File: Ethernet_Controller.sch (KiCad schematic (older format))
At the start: 33 parts, among them J1 5-2337992-8, U1 RTL8111H, Y1 ABM8G-25.000MHZ-18-D2Y-T

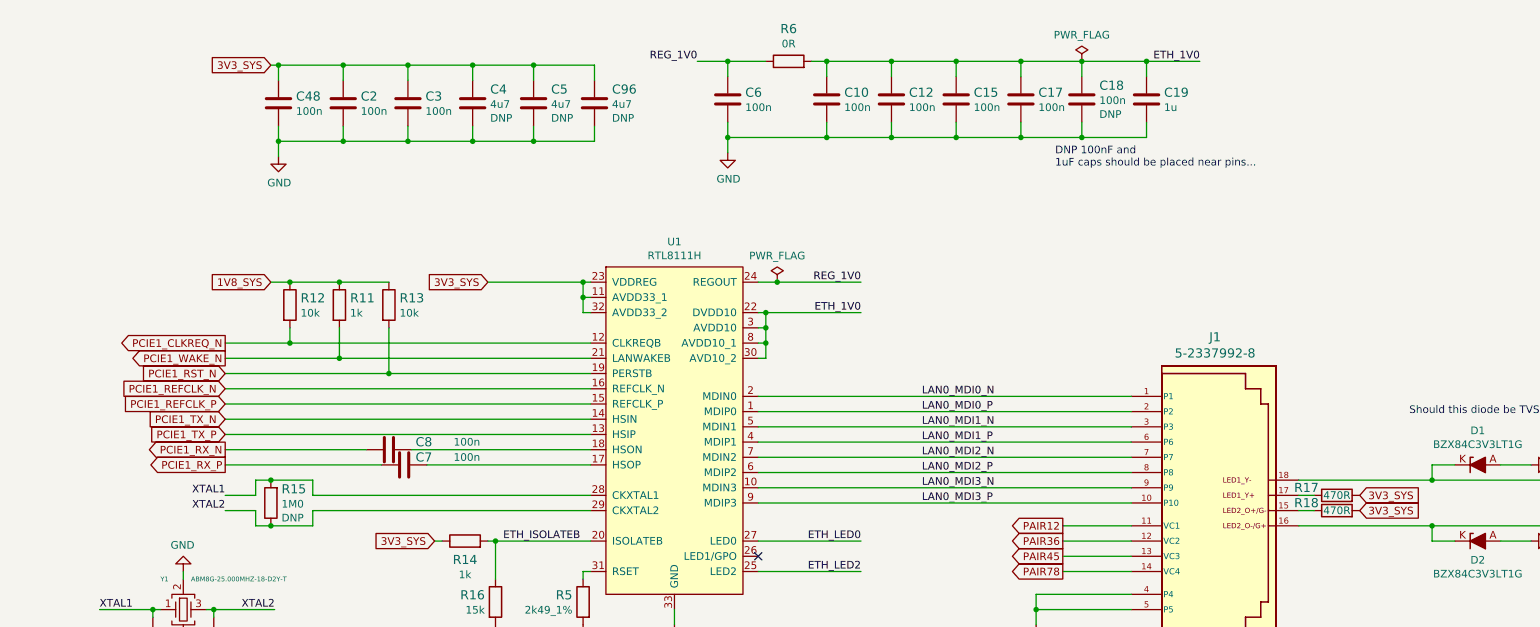
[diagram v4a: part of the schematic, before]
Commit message: Add ferrite bead to 3V3 path to ethernet, update power labels
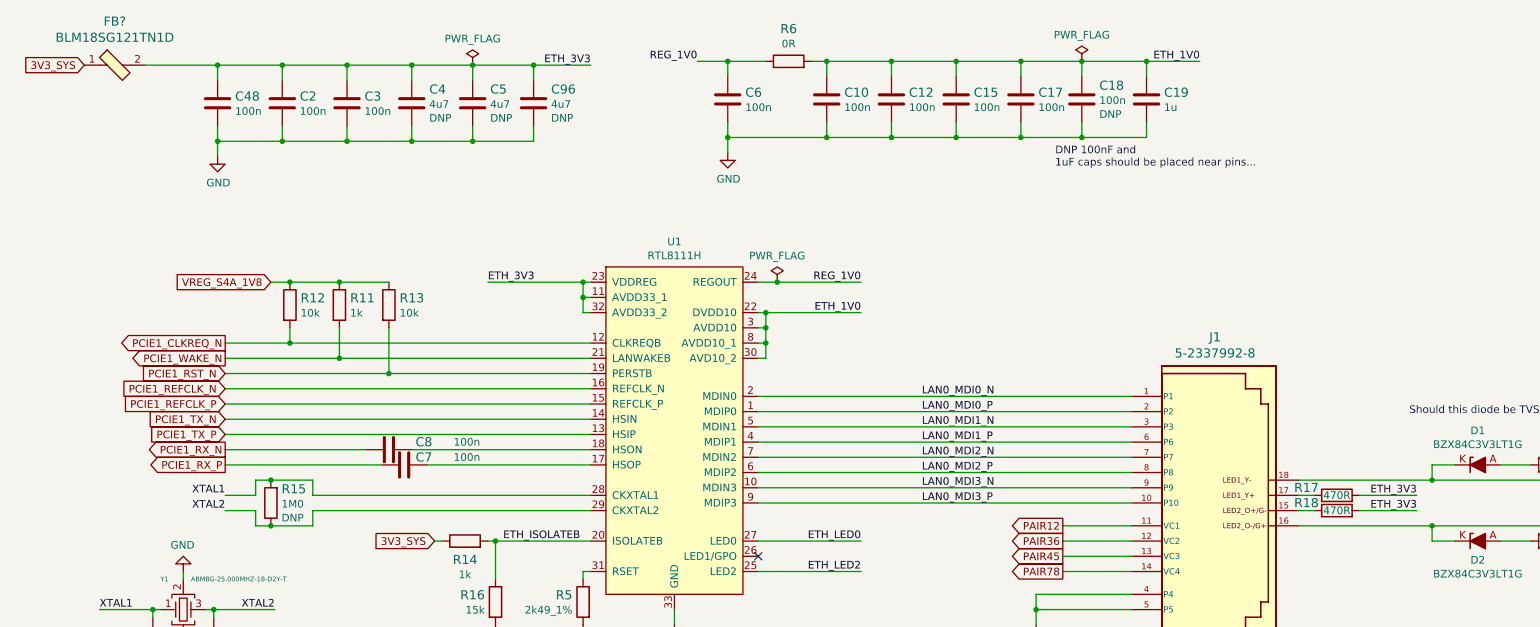
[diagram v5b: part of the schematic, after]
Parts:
- added FB?: BLM18SG121TN1D, sa800u-baseboard-hw-footprints:0603-res, symbol sa800u-baseboard-hw:BLM18SG121TN1D
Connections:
- net 3V3_SYS: now also FB?.1; no longer C2.1, C3.1, C4.1, C48.1, C5.1, C96.1, R17.2, R18.2, U1.11 (AVDD33_1), U1.23 (VDDREG), U1.32 (AVDD33_2)
- net 1V8_SYS renamed VREG_S4A_1V8
- new net ETH_3V3: C2.1, C3.1, C4.1, C48.1, C5.1, C96.1, FB?.2, R17.2, R18.2, U1.11 (AVDD33_1), U1.23 (VDDREG), U1.32 (AVDD33_2)
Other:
- moved on the sheet: C2, C3, C4, C48, C5, C96
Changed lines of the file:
@@
 Wire Wire Line
 	11700 6025 11600 6025
-Text GLabel 12000 5925 2    50   Input ~ 0
-3V3_SYS
-Text GLabel 12000 6025 2    50   Input ~ 0
-3V3_SYS
 Wire Wire Line
 	12475 6225 12475 6125
@@
 Text Notes 10675 7300 0    50   ~ 10
 Possible replacement:\nhttps://www.l-p.com/products/457392.htm
-Text GLabel 4850 3100 0    50   Input ~ 0
+Text GLabel 3625 3100 0    50   Input ~ 0
 3V3_SYS
 $Comp
 L sa800u-baseboard-hw:C_100n_0402 C2
 U 1 1 62C66184
-P 5325 3350
-F 0 "C2" H 5440 3395 60  0000 L CNN
-F 1 "C_100n_0402" H 5325 3200 60  0001 C CNN
-F 2 "sa800u-baseboard-hw-footprints:0402-cap" H 5525 3550 60  0001 L CNN
-F 3 "" H 5325 3350 50  0001 C CNN
-F 4 "Walsin" H 5525 3750 60  0001 L CNN "Manufacturer"
-F 5 "0402X104K6R3CT" H 5525 3650 60  0001 L CNN "MPN"
-F 6 "100n" H 5440 3297 50  0000 L CNN "Val"
-	1    5325 3350
+P 4925 3350
+F 0 "C2" H 5040 3395 60  0000 L CNN
+F 1 "C_100n_0402" H 4925 3200 60  0001 C CNN
+F 2 "sa800u-baseboard-hw-footprints:0402-cap" H 5125 3550 60  0001 L CNN
+F 3 "" H 4925 3350 50  0001 C CNN
+F 4 "Walsin" H 5125 3750 60  0001 L CNN "Manufacturer"
+F 5 "0402X104K6R3CT" H 5125 3650 60  0001 L CNN "MPN"
+F 6 "100n" H 5040 3297 50  0000 L CNN "Val"
+	1    4925 3350
 	1    0    0    -1
 $EndComp
@@
 L sa800u-baseboard-hw:C_100n_0402 C3
 U 1 1 62C66AB1
-P 5750 3350
-F 0 "C3" H 5865 3395 60  0000 L CNN
-F 1 "C_100n_0402" H 5750 3200 60  0001 C CNN
-F 2 "sa800u-baseboard-hw-footprints:0402-cap" H 5950 3550 60  0001 L CNN
-F 3 "" H 5750 3350 50  0001 C CNN
-F 4 "Walsin" H 5950 3750 60  0001 L CNN "Manufacturer"
-F 5 "0402X104K6R3CT" H 5950 3650 60  0001 L CNN "MPN"
-F 6 "100n" H 5865 3297 50  0000 L CNN "Val"
-	1    5750 3350
+P 5350 3350
+F 0 "C3" H 5465 3395 60  0000 L CNN
+F 1 "C_100n_0402" H 5350 3200 60  0001 C CNN
+F 2 "sa800u-baseboard-hw-footprints:0402-cap" H 5550 3550 60  0001 L CNN
+F 3 "" H 5350 3350 50  0001 C CNN
+F 4 "Walsin" H 5550 3750 60  0001 L CNN "Manufacturer"
+F 5 "0402X104K6R3CT" H 5550 3650 60  0001 L CNN "MPN"
+F 6 "100n" H 5465 3297 50  0000 L CNN "Val"
+	1    5350 3350
 	1    0    0    -1
 $EndComp
@@
 L sa800u-baseboard-hw:C_4u7_0402 C4
 U 1 1 62C67F6F
+P 5775 3350
+F 0 "C4" H 5890 3441 60  0000 L CNN
+F 1 "C_4u7_0402" H 5775 3200 60  0001 C CNN
+F 2 "sa800u-baseboard-hw-footprints:0402-cap" H 5975 3550 60  0001 L CNN
+F 3 "" H 5775 3350 50  0001 C CNN
+F 4 "MURATA" H 5975 3750 60  0001 L CNN "Manufacturer"
+F 5 "GRM155R61A475MEAAD" H 5975 3650 60  0001 L CNN "MPN"
+F 6 "4u7" H 5890 3343 50  0000 L CNN "Val"
+F 7 "DNP" H 5890 3252 50  0000 L CNN "DNP"
+	1    5775 3350
+	1    0    0    -1
+$EndComp
+$Comp
+L sa800u-baseboard-hw:C_4u7_0402 C5
+U 1 1 62C68893
 P 6175 3350
-F 0 "C4" H 6290 3441 60  0000 L CNN
+F 0 "C5" H 6290 3441 60  0000 L CNN
 F 1 "C_4u7_0402" H 6175 3200 60  0001 C CNN
 F 2 "sa800u-baseboard-hw-footprints:0402-cap" H 6375 3550 60  0001 L CNN
@@
 	1    0    0    -1
 $EndComp
-$Comp
-L sa800u-baseboard-hw:C_4u7_0402 C5
-U 1 1 62C68893
-P 6575 3350
-F 0 "C5" H 6690 3441 60  0000 L CNN
-F 1 "C_4u7_0402" H 6575 3200 60  0001 C CNN
-F 2 "sa800u-baseboard-hw-footprints:0402-cap" H 6775 3550 60  0001 L CNN
-F 3 "" H 6575 3350 50  0001 C CNN
-F 4 "MURATA" H 6775 3750 60  0001 L CNN "Manufacturer"
-F 5 "GRM155R61A475MEAAD" H 6775 3650 60  0001 L CNN "MPN"
-F 6 "4u7" H 6690 3343 50  0000 L CNN "Val"
-F 7 "DNP" H 6690 3252 50  0000 L CNN "DNP"
-	1    6575 3350
-	1    0    0    -1
-$EndComp
-Wire Wire Line
-	5750 3100 5750 3200
-Wire Wire Line
-	5325 3100 5325 3200
+Wire Wire Line
+	5350 3100 5350 3200
+Wire Wire Line
+	4925 3100 4925 3200
+Wire Wire Line
+	5775 3100 5775 3200
 Wire Wire Line
 	6175 3100 6175 3200
 Wire Wire Line
-	6575 3100 6575 3200
-Wire Wire Line
-	5325 3500 5325 3600
-Wire Wire Line
-	5750 3600 5750 3500
+	4925 3500 4925 3600
+Wire Wire Line
+	5350 3600 5350 3500
+Wire Wire Line
+	5775 3500 5775 3600
 Wire Wire Line
 	6175 3500 6175 3600
 Wire Wire Line
-	6575 3500 6575 3600
-Wire Wire Line
-	4900 3600 4900 3700
+	4500 3600 4500 3700
 $Comp
 L sa800u-baseboard-hw:GND #PWR02
 U 1 1 62C92996
-P 4900 3700
-F 0 "#PWR02" H 4900 3450 50  0001 C CNN
-F 1 "GND" H 4905 3527 50  0000 C CNN
-F 2 "" H 4900 3700 50  0001 C CNN
-F 3 "" H 4900 3700 50  0001 C CNN
-	1    4900 3700
+P 4500 3700
+F 0 "#PWR02" H 4500 3450 50  0001 C CNN
+F 1 "GND" H 4505 3527 50  0000 C CNN
+F 2 "" H 4500 3700 50  0001 C CNN
+F 3 "" H 4500 3700 50  0001 C CNN
+	1    4500 3700
 	1    0    0    -1
 $EndComp
@@
 L sa800u-baseboard-hw:C_100n_0402 C48
 U 1 1 61E50090
-P 4900 3350
-F 0 "C48" H 5015 3395 60  0000 L CNN
-F 1 "C_100n_0402" H 4900 3200 60  0001 C CNN
-F 2 "sa800u-baseboard-hw-footprints:0402-cap" H 5100 3550 60  0001 L CNN
-F 3 "" H 4900 3350 50  0001 C CNN
-F 4 "Walsin" H 5100 3750 60  0001 L CNN "Manufacturer"
-F 5 "0402X104K6R3CT" H 5100 3650 60  0001 L CNN "MPN"
-F 6 "100n" H 5015 3297 50  0000 L CNN "Val"
-	1    4900 3350
-	1    0    0    -1
-$EndComp
-Wire Wire Line
-	4900 3100 4900 3200
-Wire Wire Line
-	4900 3500 4900 3600
-Connection ~ 4900 3600
-Wire Wire Line
-	4850 3100 4900 3100
-Connection ~ 4900 3100
-Connection ~ 5325 3100
-Connection ~ 6175 3600
-Wire Wire Line
-	4900 3100 5325 3100
-Wire Wire Line
-	4900 3600 5325 3600
-Connection ~ 5750 3100
-Wire Wire Line
-	5325 3100 5750 3100
-Wire Wire Line
-	5325 3600 5750 3600
-Connection ~ 5325 3600
-Connection ~ 6175 3100
-Wire Wire Line
-	5750 3100 6175 3100
-Wire Wire Line
-	5750 3600 6175 3600
-Connection ~ 5750 3600
-Wire Wire Line
-	6175 3600 6575 3600
-Wire Wire Line
-	6175 3100 6575 3100
+P 4500 3350
+F 0 "C48" H 4615 3395 60  0000 L CNN
+F 1 "C_100n_0402" H 4500 3200 60  0001 C CNN
+F 2 "sa800u-baseboard-hw-footprints:0402-cap" H 4700 3550 60  0001 L CNN
+F 3 "" H 4500 3350 50  0001 C CNN
+F 4 "Walsin" H 4700 3750 60  0001 L CNN "Manufacturer"
+F 5 "0402X104K6R3CT" H 4700 3650 60  0001 L CNN "MPN"
+F 6 "100n" H 4615 3297 50  0000 L CNN "Val"
+	1    4500 3350
+	1    0    0    -1
+$EndComp
+Wire Wire Line
+	4500 3100 4500 3200
+Wire Wire Line
+	4500 3500 4500 3600
+Connection ~ 4500 3600
+Connection ~ 4500 3100
+Connection ~ 4925 3100
+Connection ~ 5775 3600
+Wire Wire Line
+	4500 3100 4925 3100
+Wire Wire Line
+	4500 3600 4925 3600
+Connection ~ 5350 3100
+Wire Wire Line
+	4925 3100 5350 3100
+Wire Wire Line
+	4925 3600 5350 3600
+Connection ~ 4925 3600
+Connection ~ 5775 3100
+Wire Wire Line
+	5350 3100 5775 3100
+Wire Wire Line
+	5350 3600 5775 3600
+Connection ~ 5350 3600
+Wire Wire Line
+	5775 3600 6175 3600
+Wire Wire Line
+	5775 3100 6175 3100
 $Comp
 L sa800u-baseboard-hw:C_4u7_0402 C96
 U 1 1 61EB43EC
-P 6975 3350
-F 0 "C96" H 7090 3441 60  0000 L CNN
-F 1 "C_4u7_0402" H 6975 3200 60  0001 C CNN
-F 2 "sa800u-baseboard-hw-footprints:0402-cap" H 7175 3550 60  0001 L CNN
-F 3 "" H 6975 3350 50  0001 C CNN
-F 4 "MURATA" H 7175 3750 60  0001 L CNN "Manufacturer"
-F 5 "GRM155R61A475MEAAD" H 7175 3650 60  0001 L CNN "MPN"
-F 6 "4u7" H 7090 3343 50  0000 L CNN "Val"
-F 7 "DNP" H 7090 3252 50  0000 L CNN "DNP"
-	1    6975 3350
-	1    0    0    -1
-$EndComp
-Wire Wire Line
-	6975 3100 6975 3200
-Wire Wire Line
-	6975 3500 6975 3600
-Wire Wire Line
-	6575 3600 6975 3600
-Wire Wire Line
-	6575 3100 6975 3100
-Connection ~ 6575 3100
-Connection ~ 6575 3600
+P 6575 3350
+F 0 "C96" H 6690 3441 60  0000 L CNN
+F 1 "C_4u7_0402" H 6575 3200 60  0001 C CNN
+F 2 "sa800u-baseboard-hw-footprints:0402-cap" H 6775 3550 60  0001 L CNN
+F 3 "" H 6575 3350 50  0001 C CNN
+F 4 "MURATA" H 6775 3750 60  0001 L CNN "Manufacturer"
+F 5 "GRM155R61A475MEAAD" H 6775 3650 60  0001 L CNN "MPN"
+F 6 "4u7" H 6690 3343 50  0000 L CNN "Val"
+F 7 "DNP" H 6690 3252 50  0000 L CNN "DNP"
+	1    6575 3350
+	1    0    0    -1
+$EndComp
+Wire Wire Line
+	6575 3100 6575 3200
+Wire Wire Line
+	6575 3500 6575 3600
+Wire Wire Line
+	6175 3600 6575 3600
+Wire Wire Line
+	6175 3100 6575 3100
+Connection ~ 6175 3100
+Connection ~ 6175 3600
 $Comp
 L sa800u-baseboard-hw:C_100n_0402 C10
@@
 	0    -1   1    0
 $EndComp
-Text GLabel 6275 4525 0    50   Input ~ 0
-3V3_SYS
 $Comp
 L sa800u-baseboard-hw:RTL8111H U1
@@
 	0    1    1    0
 $EndComp
-Text GLabel 4850 4525 0    50   Input ~ 0
-1V8_SYS
 $Comp
 L sa800u-baseboard-hw:R_10k_0402 R13
@@
 Wire Wire Line
 	8050 5875 10500 5875
+Text GLabel 4850 4525 0    50   Input ~ 0
+VREG_S4A_1V8
+$Comp
+L sa800u-baseboard-hw:BLM18SG121TN1D FB?
+U 1 1 631C3DCA
+P 3825 3100
+F 0 "FB?" H 3825 3387 60  0000 C CNN
+F 1 "BLM18SG121TN1D" H 3825 3281 60  0000 C CNN
+F 2 "sa800u-baseboard-hw-footprints:0603-res" H 4025 3300 60  0001 L CNN
+F 3 "https://www.murata.com/en-global/api/pdfdownloadapi?cate=luNoiseSupprFilteChipFerriBead&partno=BLM18SG121TN1%23" H 4025 3400 60  0001 L CNN
+F 4 "BLM18SG121TN1D" H 4025 3600 60  0001 L CNN "MPN"
+F 5 "Murata Electronics North America" H 4025 4200 60  0001 L CNN "Manufacturer"
+	1    3825 3100
+	1    0    0    -1
+$EndComp
+Wire Wire Line
+	4025 3100 4500 3100
+Text Label 6950 3100 2    50   ~ 0
+ETH_3V3
+Wire Wire Line
+	6575 3100 6950 3100
+Connection ~ 6575 3100
+$Comp
+L sa800u-baseboard-hw:PWR_FLAG #FLG?
+U 1 1 63216C75
+P 6175 3100
+F 0 "#FLG?" H 6175 3175 50  0001 C CNN
+F 1 "PWR_FLAG" H 6175 3273 50  0000 C CNN
+F 2 "" H 6175 3100 50  0001 C CNN
+F 3 "~" H 6175 3100 50  0001 C CNN
+	1    6175 3100
+	1    0    0    -1
+$EndComp
+Text Label 6275 4525 0    50   ~ 0
+ETH_3V3
+Text Label 12375 5925 2    50   ~ 0
+ETH_3V3
+Wire Wire Line
+	12375 5925 12000 5925
+Text Label 12375 6025 2    50   ~ 0
+ETH_3V3
+Wire Wire Line
+	12375 6025 12000 6025
 $EndSCHEMATC

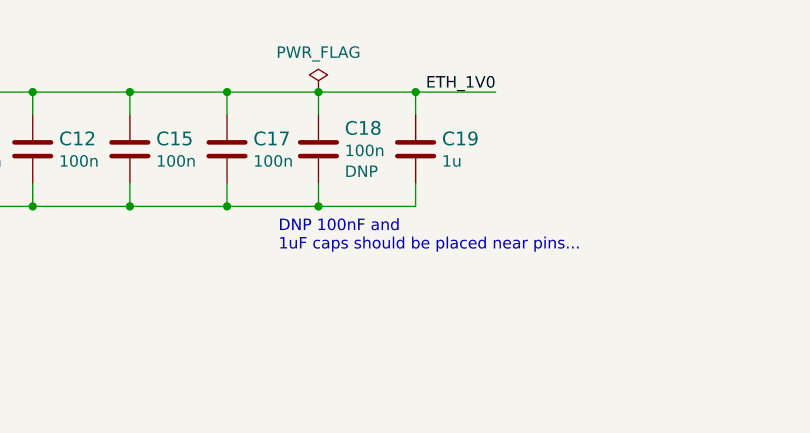
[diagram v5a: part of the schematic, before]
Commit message: Set C19 to DNP, make DNP visible. Remove C18
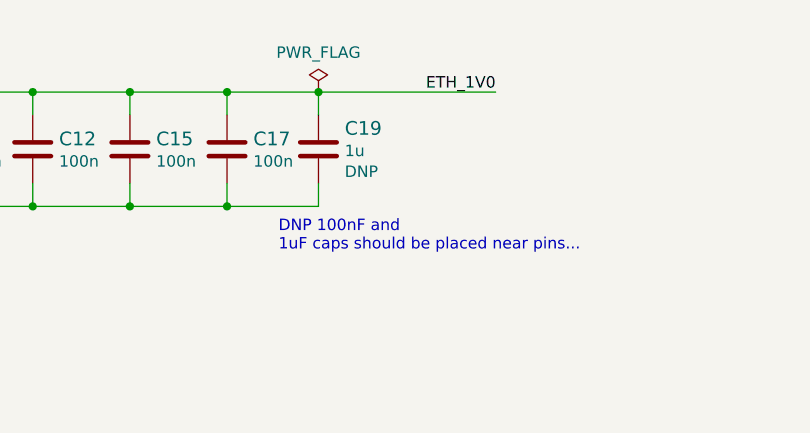
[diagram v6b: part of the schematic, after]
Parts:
- removed C18: C_100n_0402, sa800u-baseboard-hw-footprints:0402-cap, symbol sa800u-baseboard-hw:C_100n_0402
- C19: DNP (none) -> DNP
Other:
- moved on the sheet: C19
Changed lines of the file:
@@
 Wire Wire Line
 	9350 3075 9775 3075
-$Comp
-L sa800u-baseboard-hw:C_100n_0402 C18
-U 1 1 62CBADDF
+Connection ~ 10175 3075
+Wire Wire Line
+	9775 3075 10175 3075
+$Comp
+L sa800u-baseboard-hw:C_1u_0402 C19
+U 1 1 62CDD350
 P 10175 3325
-F 0 "C18" H 10290 3416 60  0000 L CNN
-F 1 "C_100n_0402" H 10175 3175 60  0001 C CNN
+F 0 "C19" H 10290 3416 60  0000 L CNN
+F 1 "C_1u_0402" H 10175 3175 60  0001 C CNN
 F 2 "sa800u-baseboard-hw-footprints:0402-cap" H 10375 3525 60  0001 L CNN
 F 3 "" H 10175 3325 50  0001 C CNN
-F 4 "Walsin" H 10375 3725 60  0001 L CNN "Manufacturer"
-F 5 "0402X104K6R3CT" H 10375 3625 60  0001 L CNN "MPN"
-F 6 "100n" H 10290 3318 50  0000 L CNN "Val"
+F 4 "TDK" H 10375 3725 60  0001 L CNN "Manufacturer"
+F 5 "C1005X6S1A105K050BC" H 10375 3625 60  0001 L CNN "MPN"
+F 6 "1u" H 10290 3318 50  0000 L CNN "Val"
 F 7 "DNP" H 10290 3227 50  0000 L CNN "DNP"
 	1    10175 3325
@@
 $EndComp
 Wire Wire Line
+	10175 3175 10175 3075
+Wire Wire Line
 	10175 3575 10175 3475
-Wire Wire Line
-	10175 3175 10175 3075
-Connection ~ 10175 3075
-Connection ~ 10175 3575
-Wire Wire Line
-	9775 3575 10175 3575
-Wire Wire Line
-	9775 3075 10175 3075
-$Comp
-L sa800u-baseboard-hw:C_1u_0402 C19
-U 1 1 62CDD350
-P 10600 3325
-F 0 "C19" H 10715 3370 60  0000 L CNN
-F 1 "C_1u_0402" H 10600 3175 60  0001 C CNN
-F 2 "sa800u-baseboard-hw-footprints:0402-cap" H 10800 3525 60  0001 L CNN
-F 3 "" H 10600 3325 50  0001 C CNN
-F 4 "TDK" H 10800 3725 60  0001 L CNN "Manufacturer"
-F 5 "C1005X6S1A105K050BC" H 10800 3625 60  0001 L CNN "MPN"
-F 6 "1u" H 10715 3272 50  0000 L CNN "Val"
-	1    10600 3325
-	1    0    0    -1
-$EndComp
-Wire Wire Line
-	10600 3175 10600 3075
-Wire Wire Line
-	10600 3575 10600 3475
-Wire Wire Line
-	10175 3575 10600 3575
-Connection ~ 10600 3075
-Wire Wire Line
-	10175 3075 10600 3075
 Text Label 10950 3075 2    50   ~ 0
 ETH_1V0
-Wire Wire Line
-	10600 3075 10950 3075
 Wire Wire Line
 	7650 3075 7850 3075
@@
 Wire Wire Line
 	12375 6025 12000 6025
+Wire Wire Line
+	9775 3575 10175 3575
+Wire Wire Line
+	10175 3075 10950 3075
 $EndSCHEMATC
